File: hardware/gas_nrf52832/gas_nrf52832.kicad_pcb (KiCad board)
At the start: 4 copper layers, 64 x 35 mm, 83 parts, among them IC1 REF1112AIDBZR, IC3 LPV821DBVR, IC4 LPV821DBVR, IC5 LPV821DBVR, IC6 NPM1100-QDAA-R, J1 J-link, J3 Batt_SW, J4 Conn_01x03, J5 USB4515-GF-A, Q3 FDV303N, Q4 DMC2400UV-7, U3 MMBFJ177, U5 BME680, X1 32.768kHz

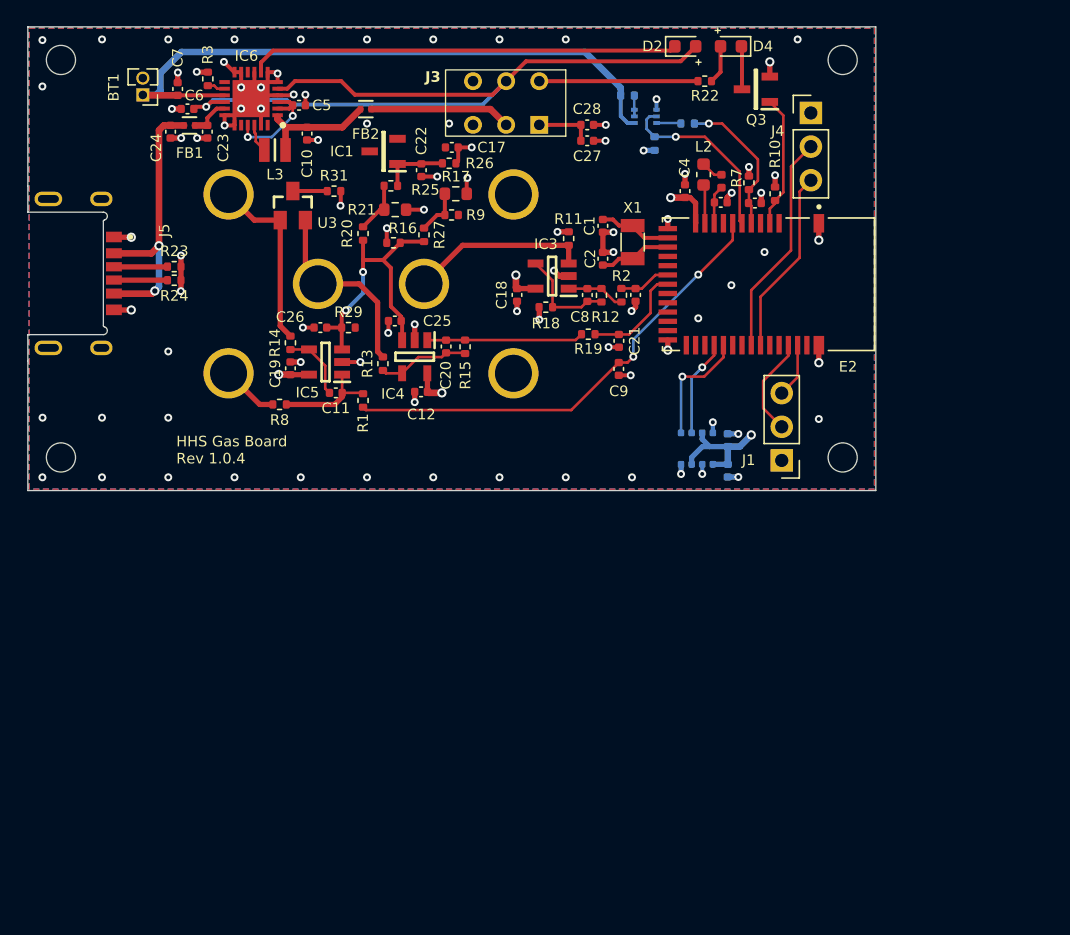
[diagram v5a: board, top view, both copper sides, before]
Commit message: feat: hw revision 2.0.1
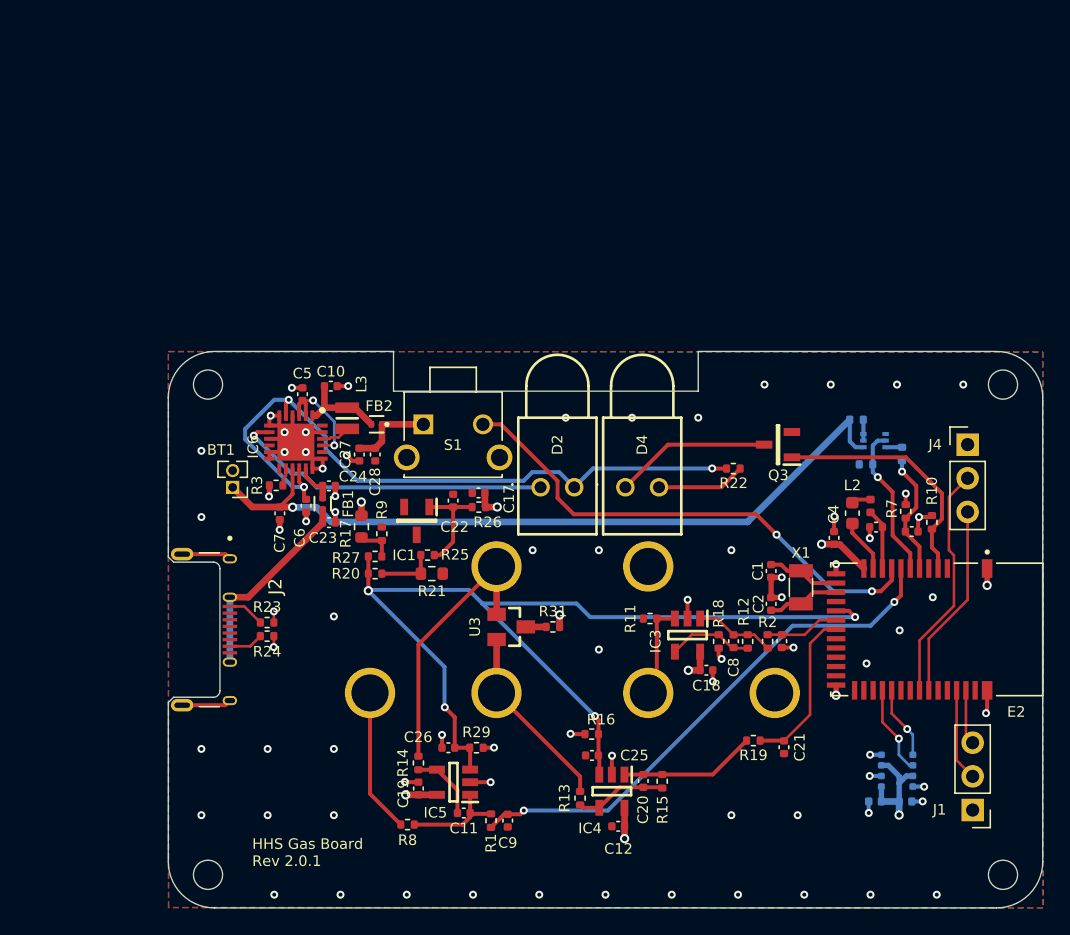
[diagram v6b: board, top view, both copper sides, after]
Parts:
- removed J3: Batt_SW, HHS:MSL-1C2P
- removed J5: USB4515-GF-A, USB4515-GF-A_REVA:GCT_USB4515-GF-A_REVA
- added J2: USB, UJ20-C-G-MSMT-TR-68:CUI_UJ20-C-G-MSMT-TR-68, F.Cu at (101.0, 121.0)
- added S1: SW1, TS11-674-43-BK-100-RA-D:SW_TS11-674-43-BK-100-RA-D, F.Cu at (121.5, 105.5)
- C23: value 10nF -> 100nF
- C24: value 100nF -> 10nF
- D2, D4: footprint LED_SMD:LED_0603_1608Metric -> WP1533BQ_ID:WP1533BQ
- moved R16 40.0 mm to (132.0, 128.9)
- moved R31 36.8 mm to (129.0, 120.8)
- moved C12 36.0 mm to (134.0, 135.8)
- moved R13 36.0 mm to (131.1, 133.7)
- moved C25 36.0 mm to (132.0, 130.5)
- moved C20 36.0 mm to (135.8, 132.4)
- moved IC4 36.0 mm to (133.5, 133.2)
- moved R15 36.0 mm to (137.3, 132.4)
- moved U3 35.8 mm to (125.9, 120.8), turned to -90 degrees
- moved C9 35.1 mm to (125.6, 135.4)
- moved D2 35.0 mm to (128.1, 110.2), turned to -90 degrees
- moved D4 34.2 mm to (134.5, 110.2), turned to -90 degrees
- moved C11 33.1 mm to (122.3, 134.8)
- moved C19 33.1 mm to (118.9, 133.0)
- moved R14 33.1 mm to (118.9, 131.1)
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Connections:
- C23 pad 2: VBUS -> Net-(J2-VBUS)
- C24 pad 2: Net-(C24-Pad2) -> VBUS
- E2 pad 16: unconnected-(E2-P0.03/AIN1-Pad16) -> Vref
- E2 pad 8: unconnected-(E2-P0.31/AIN7-Pad8) -> POWER
- FB1 pad 1: Net-(C24-Pad2) -> Net-(J2-VBUS)
- FB2 pad 2: Net-(J3-Pin_2) -> VDD_nRF
- R22 pad 2: VSYS -> VSYS_RAW
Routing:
- net Vref: track 21.9 -> 75.8 mm, vias 2 -> 4
- net POWER: track 0.00 -> 38.1 mm, vias 0 -> 2
- net Net-(C24-Pad2): track 21.1 -> 0.00 mm, vias 2 -> 0
- net Net-(J2-VBUS): track 0.00 -> 15.3 mm
- net VSYS: track 12.0 -> 0.00 mm
- net Net-(J3-Pin_2): track 10.7 -> 0.00 mm
- net NORMAL: track 10.0 -> 18.6 mm
- net Net-(D4-K): track 3.26 -> 11.8 mm
- net VBAT: track 48.9 -> 57.0 mm, vias 0 -> 1
- net Net-(D2-K): track 32.5 -> 24.6 mm, vias 0 -> 1
- net VSYS_RAW: track 60.0 -> 52.2 mm, vias 1 -> 3
- net Net-(R14-Pad2): track 13.8 -> 20.4 mm
- net Net-(R8-Pad2): track 4.31 -> 10.9 mm
- net Net-(IC3-+IN): track 13.5 -> 7.25 mm
- net GND: track 68.5 -> 63.4 mm, vias 87 -> 77
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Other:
- board size 64 x 35 mm -> 66 x 42 mm
- board text added: "HHS Gas Board Rev 2.0.1"
- board text removed: "HHS Gas Board Rev 1.0.4"
